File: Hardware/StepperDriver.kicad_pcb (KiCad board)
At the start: 6 copper layers, 50 x 50 mm, 60 parts, among them J1 DC, J2 MOTOR, J3 OLED, J4 JTAG, SW1 SPST_TS, SW2 SPST_TS, SW3 SPST_TS, U1 TPS5430DDA, U2 TMC2208-LA, U3 XIAO-ESP32C6

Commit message: Driver update
Moved to the better TMC2209 stepper motor driver.
Added a status LED for the voltage regulator.
Updated the output files.
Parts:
- added D5: RED, LED_SMD:LED_0603_1608Metric, F.Cu at (172.2, 91.3)
- added G***: LOGO, Custom_Parts:OSHW, B.Cu at (150.0, 83.6)
- added R13: 2.2K, Resistor_SMD:R_0603_1608Metric, F.Cu at (169.0, 91.3)
- U2: value TMC2208-LA -> TMC2209-LA; footprint Custom_Parts:QFN-28-1EP_5x5mm_P0.5mm_EP3.1x3.1mm_ThermalVias -> Custom_Parts:VQFN-28-1EP_5x5mm_P0.5mm_EP3.7x3.7mm_ThermalVias
- renumbered R13 to R14, R14 to R15, R15 to R16
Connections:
- U2 pad 20: unconnected-(U2-NC-Pad20) -> GND
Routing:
- net /M_B2: track 2.78 -> 25.0 mm
- net /M_A2: track 2.78 -> 19.3 mm
- net /M_B1: track 2.78 -> 16.5 mm
- net /M_A1: track 2.78 -> 16.1 mm
- net /LED_5V: track 0.00 -> 1.59 mm
- net GND: track 12.4 -> 13.9 mm, vias 109 -> 108
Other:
- board text added: "XIAO BOARD COMPATIBLE"

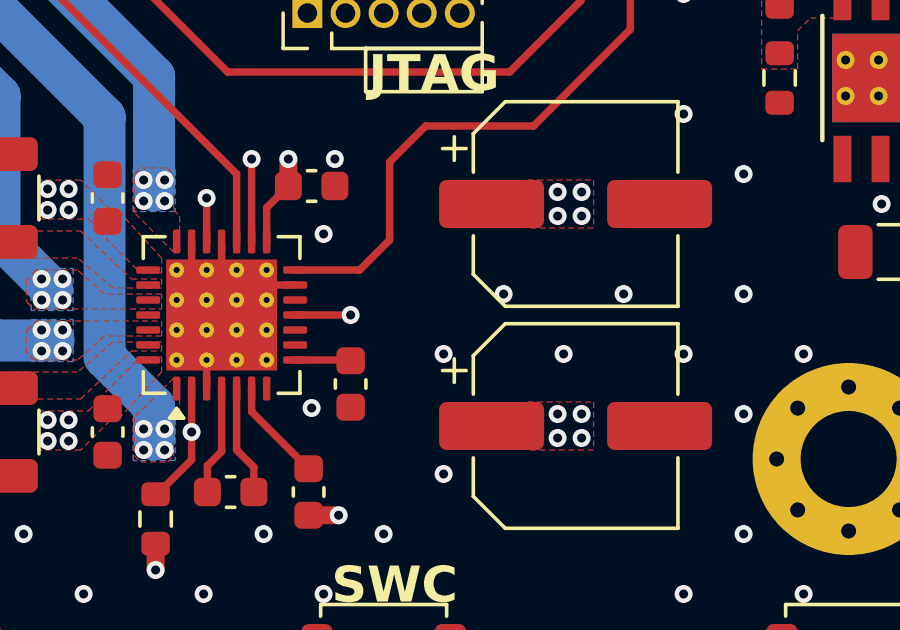
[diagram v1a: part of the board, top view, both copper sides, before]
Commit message: Output files
Minor changes on the PCB.
Updated the bulk capacitors for the board to have a lower voltage rating.
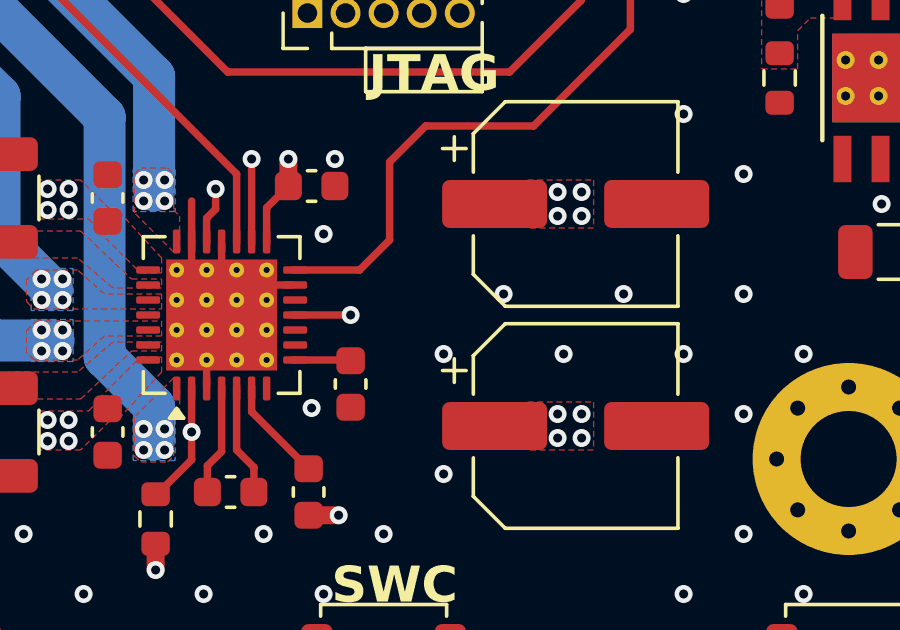
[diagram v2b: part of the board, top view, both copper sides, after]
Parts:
- C4, C5: footprint Capacitor_SMD:CP_Elec_6.3x5.4 -> Capacitor_SMD:CP_Elec_6.3x5.8
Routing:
- net GND: track 13.9 -> 15.2 mm

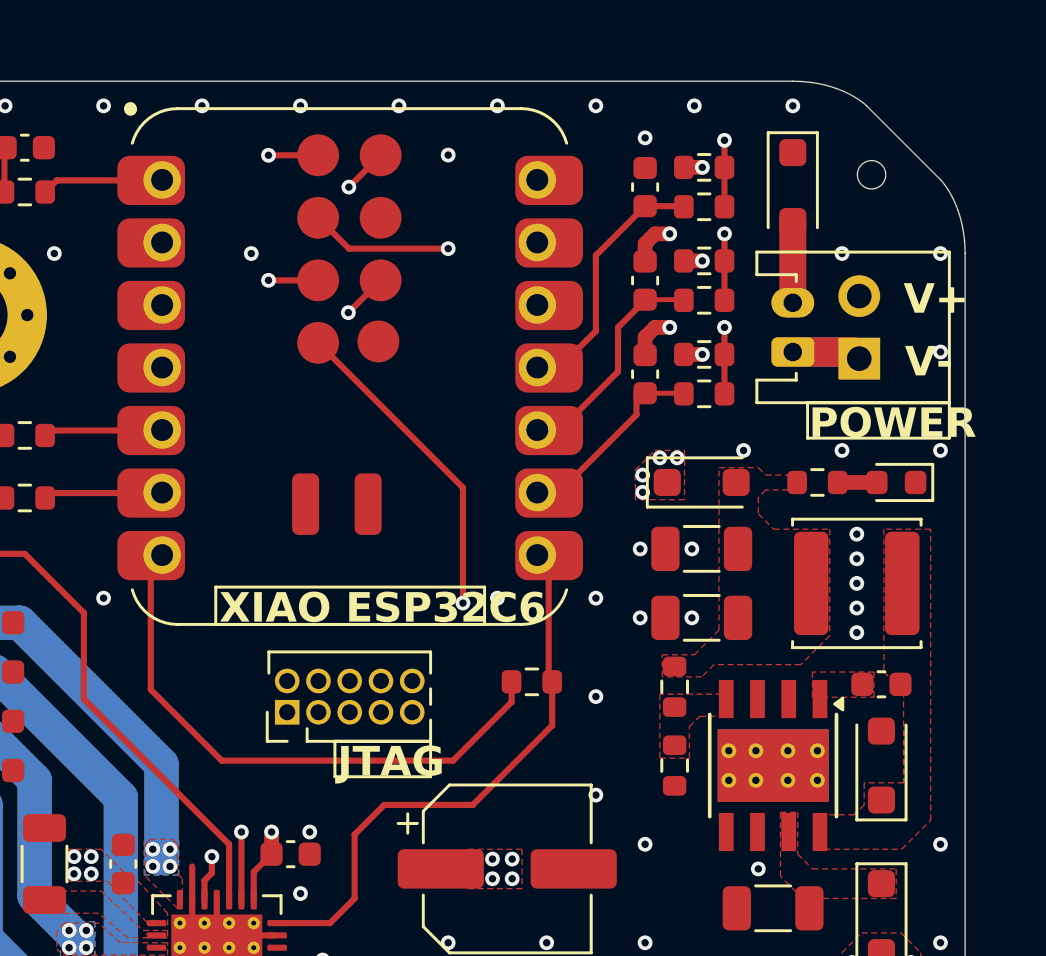
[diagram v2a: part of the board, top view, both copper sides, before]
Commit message: Output files
Minor changes to the board and schematic.
Updated the output files.
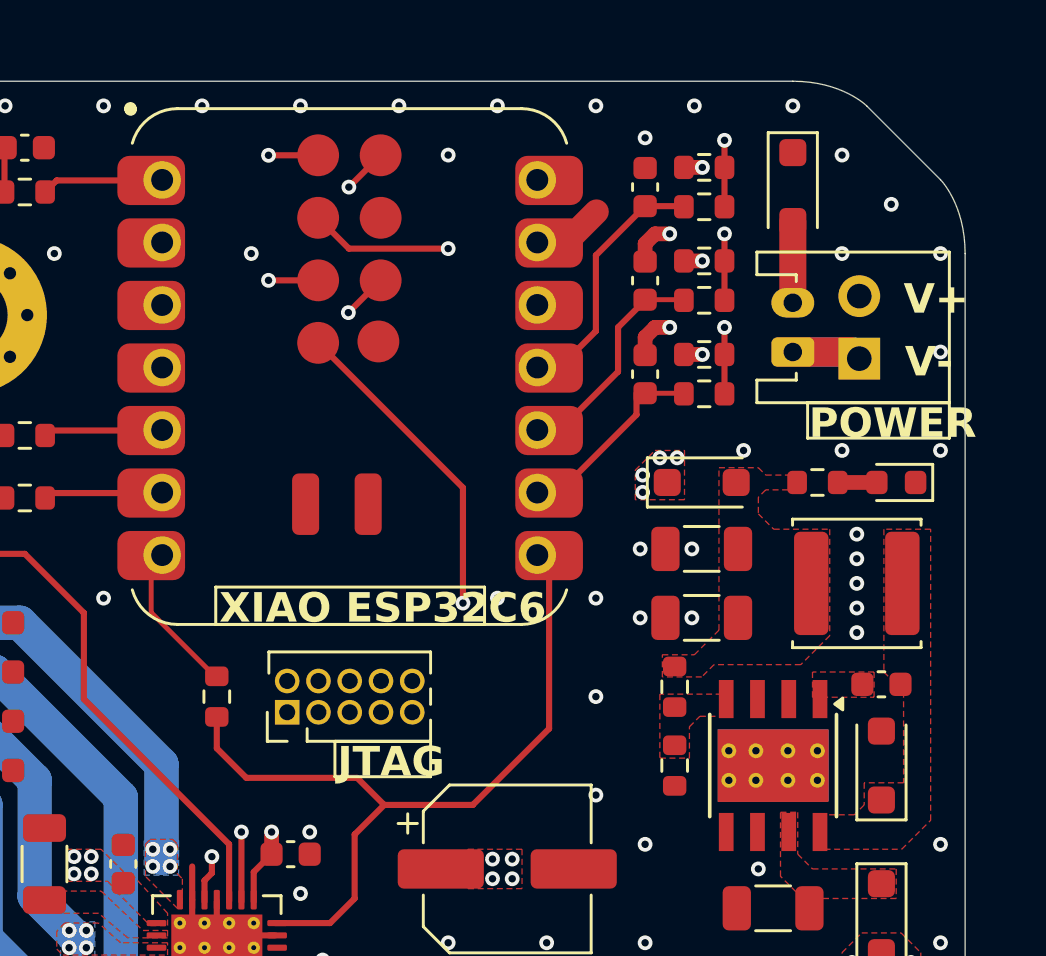
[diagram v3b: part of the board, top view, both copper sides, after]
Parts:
- removed H4: TOOL, MountingHole:ToolingHole_1.152mm
- R9: value 1K -> 0R
- moved R9 12.8 mm to (144.6, 100.0), turned to 90 degrees
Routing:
- net /TX: track 23.1 -> 6.51 mm
- net /DRV_UART: track 22.9 -> 32.0 mm
- net GND: track 15.2 -> 18.2 mm, vias 108 -> 110

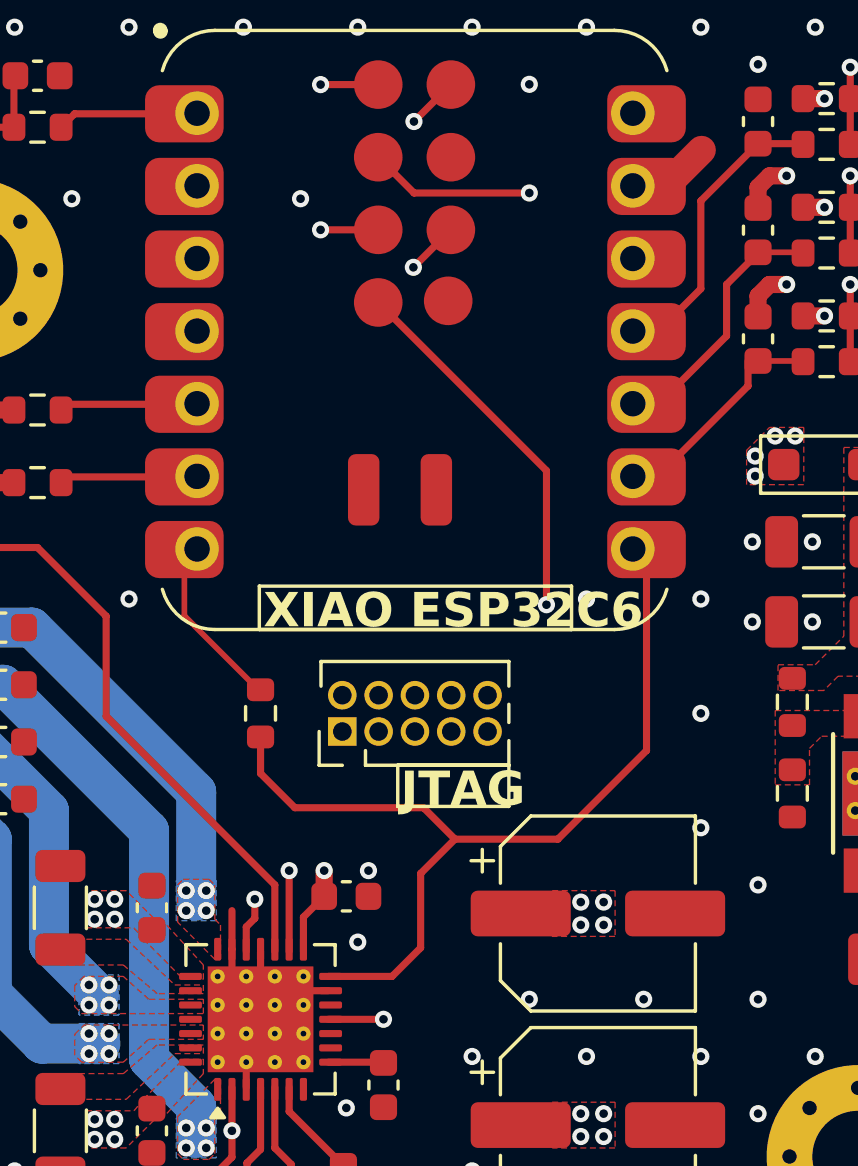
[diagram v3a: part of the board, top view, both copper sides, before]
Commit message: Assembly review
Performed a full review of the schematic and layout.
Minor changes to the schematic and layout.
Updated output files.
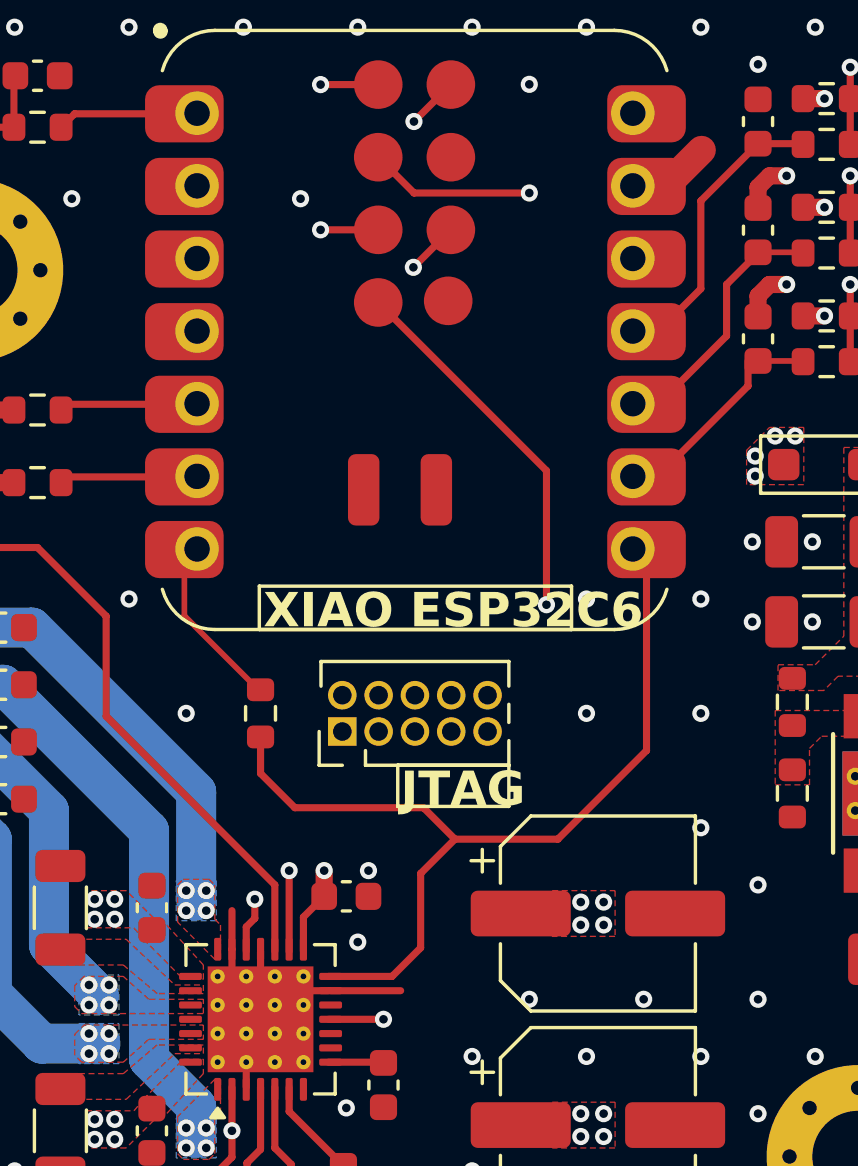
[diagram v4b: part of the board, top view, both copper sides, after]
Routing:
- net GND: track 18.2 -> 19.5 mm, vias 110 -> 112
- net /TX: track 6.51 -> 5.98 mm
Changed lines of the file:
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@@
 	)
 	(gr_rect
-		(start 160.166587 90.246203)
-		(end 173 103.1)
+		(start 160.166587 90.046203)
+		(end 173 102.9)
 		(stroke
 			(width 0.12)
@@
 	)
 	(barcode
-		(at 166.6 96.7 0)
+		(at 166.6 96.5 0)
 		(layer "B.SilkS")
 		(size 12 12)
@@
 	)
 	(segment
-		(start 157.62 81.55)
-		(end 158.775 81.55)
-		(width 1)
-		(layer "F.Cu")
-		(net "GND")
-	)
-	(segment
 		(start 162.4 81.2)
 		(end 163 81.2)
@@
 	)
 	(segment
+		(start 147.05 109.7)
+		(end 149.5 109.7)
+		(width 0.25)
+		(layer "F.Cu")
+		(net "GND")
+	)
+	(segment
 		(start 162 82.325)
 		(end 162 81.6)
@@
 	)
 	(via
+		(at 156 100)
+		(size 0.6)
+		(drill 0.3)
+		(layers "F.Cu" "B.Cu")
+		(free yes)
+		(net "GND")
+	)
+	(via
 		(at 148 120)
 		(size 0.6)
@@
 	)
 	(via
+		(at 142 100)
+		(size 0.6)
+		(drill 0.3)
+		(layers "F.Cu" "B.Cu")
+		(free yes)
+		(net "GND")
+	)
+	(via
 		(at 140 120)
 		(size 0.6)
@@
 	)
 	(segment
-		(start 141.955 94.25)
-		(end 141.935 94.27)
-		(width 0.2)
-		(layer "F.Cu")
-		(net "/TX")
-	)
-	(segment
 		(start 141.935 96.585)
 		(end 144.525 99.175)
 		(width 0.2)
 		(layer "F.Cu")
-		(net "/TX")
-	)
-	(segment
-		(start 144.525 99.175)
-		(end 144.6 99.175)
-		(width 0.2)
-		(layer "F.Cu")
-		(net "/TX")
-	)
-	(segment
-		(start 142.38 94.25)
-		(end 141.955 94.25)
-		(width 0.2)
-		(layer "F.Cu")
